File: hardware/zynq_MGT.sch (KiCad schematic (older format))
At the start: 6 parts, among them U201 xc7z030sbg485

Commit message: Layouted most of the Power Circuit and Triggerbus Levelshifters.
Added Footprint for Tantal Caps. Modified Footprint for MDR20 Connector, SD-Card.

Fixed Symbol and Circuit for Power Supervisor/Delay IC.

Also fixed some smaller things in the schematics.
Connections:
- wire segments 29 -> 30
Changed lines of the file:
@@
 $EndComp
 Wire Wire Line
-	5200 2150 5350 2150
+	5200 2150 5300 2150
 Wire Wire Line
 	5350 2650 4850 2650
@@
 	5300 1950 5300 2150
 Connection ~ 5300 2150
+Wire Wire Line
+	5300 2150 5350 2150
 $EndSCHEMATC

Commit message: Layouted USB-UART.
Also moved USB-OTG to the right Side of the Board. To get there
some free Space, i moved the DDR3/Memory and the FPGA a few
Millimeters down.
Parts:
- R1001: footprint (none) -> Resistor_SMD:R_0402_1005Metric
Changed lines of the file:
@@
 F 0 "R1001" H 5130 2170 50  0000 L CNN
 F 1 "100Ω, 1%" V 5000 1950 50  0000 L CNN
-F 2 "" H 5100 2150 50  0001 C CNN
+F 2 "Resistor_SMD:R_0402_1005Metric" H 5100 2150 50  0001 C CNN
 F 3 "" H 5100 2150 50  0001 C CNN
 	1    5100 2150

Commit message: Improved Powerdistribution Network of the FPGA.
Also started to layout USB.
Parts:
- C1001, C1002, C1003, C1004: footprint Capacitors_SMD:C_0402 -> Capacitor_SMD:C_0402_1005Metric
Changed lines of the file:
@@
 F 0 "C1004" H 4260 2620 50  0000 L CNN
 F 1 "C_Small" H 4260 2470 50  0000 L CNN
-F 2 "Capacitors_SMD:C_0402" H 4250 2550 50  0001 C CNN
+F 2 "Capacitor_SMD:C_0402_1005Metric" H 4250 2550 50  0001 C CNN
 F 3 "" H 4250 2550 50  0000 C CNN
 	1    4250 2550
@@
 F 0 "C1003" H 4010 2520 50  0000 L CNN
 F 1 "C_Small" H 4010 2370 50  0000 L CNN
-F 2 "Capacitors_SMD:C_0402" H 4000 2450 50  0001 C CNN
+F 2 "Capacitor_SMD:C_0402_1005Metric" H 4000 2450 50  0001 C CNN
 F 3 "" H 4000 2450 50  0000 C CNN
 	1    4000 2450
@@
 F 0 "C1001" H 3510 2320 50  0000 L CNN
 F 1 "C_Small" H 3510 2170 50  0000 L CNN
-F 2 "Capacitors_SMD:C_0402" H 3500 2250 50  0001 C CNN
+F 2 "Capacitor_SMD:C_0402_1005Metric" H 3500 2250 50  0001 C CNN
 F 3 "" H 3500 2250 50  0000 C CNN
 	1    3500 2250
@@
 F 0 "C1002" H 3760 2420 50  0000 L CNN
 F 1 "C_Small" H 3760 2270 50  0000 L CNN
-F 2 "Capacitors_SMD:C_0402" H 3750 2350 50  0001 C CNN
+F 2 "Capacitor_SMD:C_0402_1005Metric" H 3750 2350 50  0001 C CNN
 F 3 "" H 3750 2350 50  0000 C CNN
 	1    3750 2350

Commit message: Fixed Schematic Symbols
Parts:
- C1001, C1002, C1003, C1004: symbol device:C_Small -> Device:C_Small
- R1001: symbol device:R_Small -> Device:R_Small
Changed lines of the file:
@@
 $Descr A4 11693 8268
 encoding utf-8
-Sheet 10 22
+Sheet 10 21
 Title ""
 Date ""
@@
 MGTREFCLK_1_P
 $Comp
-L device:C_Small C1004
+L Device:C_Small C1004
 U 1 1 598A74A2
 P 4250 2550
@@
 $EndComp
 $Comp
-L device:C_Small C1003
+L Device:C_Small C1003
 U 1 1 598A7543
 P 4000 2450
@@
 $EndComp
 $Comp
-L device:C_Small C1001
+L Device:C_Small C1001
 U 1 1 598A7566
 P 3500 2250
@@
 $EndComp
 $Comp
-L device:C_Small C1002
+L Device:C_Small C1002
 U 1 1 598A75B1
 P 3750 2350
@@
 MGTX_TX_0_P
 $Comp
-L device:R_Small R1001
+L Device:R_Small R1001
 U 1 1 5ADF6841
 P 5100 2150

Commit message: Xaui lanes
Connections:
- net MGTX_RX_0_N: now also U201.AB9 (MGTXRXN2_112_N); no longer U201.AB7 (MGTXRXN0_112_N)
- net MGTX_RX_0_P: now also U201.AA9 (MGTXRXP2_112_P); no longer U201.AA7 (MGTXRXP0_112_P)
- net MGTX_RX_2_N: now also U201.AB7 (MGTXRXN0_112_N); no longer U201.AB9 (MGTXRXN2_112_N)
- net MGTX_RX_2_P: now also U201.AA7 (MGTXRXP0_112_P); no longer U201.AA9 (MGTXRXP2_112_P)
- net MGTX_TX_0_N: now also U201.AA5 (MGTXTXP2_112_P); no longer U201.AB3 (MGTXTXN0_112_N)
- net MGTX_TX_0_P: now also U201.AB5 (MGTXTXN2_112_N); no longer U201.AA3 (MGTXTXP0_112_P)
- net MGTX_TX_1_N: now also U201.W4 (MGTXTXP1_112_P); no longer U201.Y4 (MGTXTXN1_112_N)
- net MGTX_TX_1_P: now also U201.Y4 (MGTXTXN1_112_N); no longer U201.W4 (MGTXTXP1_112_P)
- net MGTX_TX_2_N: now also U201.AA3 (MGTXTXP0_112_P); no longer U201.AB5 (MGTXTXN2_112_N)
- net MGTX_TX_2_P: now also U201.AB3 (MGTXTXN0_112_N); no longer U201.AA5 (MGTXTXP2_112_P)
- net MGTX_TX_3_N: now also U201.W2 (MGTXTXP3_112_P); no longer U201.Y2 (MGTXTXN3_112_N)
- net MGTX_TX_3_P: now also U201.Y2 (MGTXTXN3_112_N); no longer U201.W2 (MGTXTXP3_112_P)
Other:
- note added: "Pair 2 and 0 have been swapped, to ease routing"
- note added: "TX Polarity has been swapped to ease routing"
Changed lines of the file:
@@
 	1    0    0    -1
 $EndComp
-Text HLabel 3300 2750 0    60   Input ~ 0
+Text HLabel 3300 2950 0    60   Input ~ 0
 MGTX_RX_0_N
 Text HLabel 3300 2850 0    60   Input ~ 0
 MGTX_RX_1_N
-Text HLabel 3300 2950 0    60   Input ~ 0
+Text HLabel 3300 2750 0    60   Input ~ 0
 MGTX_RX_2_N
 Text HLabel 3300 3050 0    60   Input ~ 0
 MGTX_RX_3_N
-Text HLabel 3300 3150 0    60   Input ~ 0
+Text HLabel 3300 3350 0    60   Input ~ 0
 MGTX_RX_0_P
 Text HLabel 3300 3250 0    60   Input ~ 0
 MGTX_RX_1_P
-Text HLabel 3300 3350 0    60   Input ~ 0
+Text HLabel 3300 3150 0    60   Input ~ 0
 MGTX_RX_2_P
 Text HLabel 3300 3450 0    60   Input ~ 0
 MGTX_RX_3_P
+Text HLabel 3300 4150 0    60   Output ~ 0
+MGTX_TX_0_N
+Text HLabel 3300 4050 0    60   Output ~ 0
+MGTX_TX_1_N
+Text HLabel 3300 3950 0    60   Output ~ 0
+MGTX_TX_2_N
+Text HLabel 3300 4250 0    60   Output ~ 0
+MGTX_TX_3_N
+Text HLabel 3300 3750 0    60   Output ~ 0
+MGTX_TX_0_P
+Text HLabel 3300 3650 0    60   Output ~ 0
+MGTX_TX_1_P
 Text HLabel 3300 3550 0    60   Output ~ 0
-MGTX_TX_0_N
-Text HLabel 3300 3650 0    60   Output ~ 0
-MGTX_TX_1_N
-Text HLabel 3300 3750 0    60   Output ~ 0
-MGTX_TX_2_N
+MGTX_TX_2_P
 Text HLabel 3300 3850 0    60   Output ~ 0
-MGTX_TX_3_N
-Text HLabel 3300 3950 0    60   Output ~ 0
-MGTX_TX_0_P
-Text HLabel 3300 4050 0    60   Output ~ 0
-MGTX_TX_1_P
-Text HLabel 3300 4150 0    60   Output ~ 0
-MGTX_TX_2_P
-Text HLabel 3300 4250 0    60   Output ~ 0
 MGTX_TX_3_P
 Text HLabel 3300 2250 0    60   Input ~ 0
@@
 	3300 2550 4150 2550
 Wire Wire Line
+	3300 2950 5350 2950
+Wire Wire Line
+	5350 2850 3300 2850
+Wire Wire Line
 	3300 2750 5350 2750
 Wire Wire Line
-	5350 2850 3300 2850
-Wire Wire Line
-	3300 2950 5350 2950
-Wire Wire Line
 	5350 3050 3300 3050
 Wire Wire Line
+	3300 3350 5350 3350
+Wire Wire Line
+	5350 3250 3300 3250
+Wire Wire Line
 	3300 3150 5350 3150
 Wire Wire Line
-	5350 3250 3300 3250
-Wire Wire Line
-	3300 3350 5350 3350
-Wire Wire Line
 	5350 3450 3300 3450
 Wire Wire Line
+	3300 4150 5350 4150
+Wire Wire Line
+	5350 4050 3300 4050
+Wire Wire Line
+	3300 3950 5350 3950
+Wire Wire Line
+	5350 4250 3300 4250
+Wire Wire Line
+	3300 3750 5350 3750
+Wire Wire Line
+	5350 3650 3300 3650
+Wire Wire Line
 	3300 3550 5350 3550
 Wire Wire Line
-	5350 3650 3300 3650
-Wire Wire Line
-	3300 3750 5350 3750
-Wire Wire Line
 	5350 3850 3300 3850
-Wire Wire Line
-	3300 3950 5350 3950
-Wire Wire Line
-	5350 4050 3300 4050
-Wire Wire Line
-	3300 4150 5350 4150
-Wire Wire Line
-	5350 4250 3300 4250
 Text Label 5250 2850 2    60   ~ 0
 MGTX_RX_1_N
-Text Label 5250 2950 2    60   ~ 0
+Text Label 5250 2750 2    60   ~ 0
 MGTX_RX_2_N
 Text Label 5250 3050 2    60   ~ 0
@@
 Text Label 5250 3250 2    60   ~ 0
 MGTX_RX_1_P
-Text Label 5250 3350 2    60   ~ 0
+Text Label 5250 3150 2    60   ~ 0
 MGTX_RX_2_P
 Text Label 5250 3450 2    60   ~ 0
 MGTX_RX_3_P
+Text Label 5250 4050 2    60   ~ 0
+MGTX_TX_1_N
+Text Label 5250 3950 2    60   ~ 0
+MGTX_TX_2_N
+Text Label 5250 4250 2    60   ~ 0
+MGTX_TX_3_N
 Text Label 5250 3650 2    60   ~ 0
-MGTX_TX_1_N
+MGTX_TX_1_P
+Text Label 5250 3550 2    60   ~ 0
+MGTX_TX_2_P
+Text Label 5250 3850 2    60   ~ 0
+MGTX_TX_3_P
+Text Label 5250 3350 2    60   ~ 0
+MGTX_RX_0_P
+Text Label 5250 2950 2    60   ~ 0
+MGTX_RX_0_N
+Text Label 5250 4150 2    60   ~ 0
+MGTX_TX_0_N
 Text Label 5250 3750 2    60   ~ 0
-MGTX_TX_2_N
-Text Label 5250 3850 2    60   ~ 0
-MGTX_TX_3_N
-Text Label 5250 4050 2    60   ~ 0
-MGTX_TX_1_P
-Text Label 5250 4150 2    60   ~ 0
-MGTX_TX_2_P
-Text Label 5250 4250 2    60   ~ 0
-MGTX_TX_3_P
-Text Label 5250 3150 2    60   ~ 0
-MGTX_RX_0_P
-Text Label 5250 2750 2    60   ~ 0
-MGTX_RX_0_N
-Text Label 5250 3550 2    60   ~ 0
-MGTX_TX_0_N
-Text Label 5250 3950 2    60   ~ 0
 MGTX_TX_0_P
 $Comp
@@
 Wire Wire Line
 	5300 2150 5350 2150
+Wire Notes Line
+	2550 3500 5300 3500
+Wire Notes Line
+	5300 3500 5300 4350
+Wire Notes Line
+	5300 4350 2550 4350
+Wire Notes Line
+	2550 4350 2550 3500
+Text Notes 3200 4500 0    50   ~ 0
+TX Polarity has been swapped to ease routing
+Text Notes 500  3100 0    50   ~ 0
+Pair 2 and 0 have been swapped, to ease routing
 $EndSCHEMATC

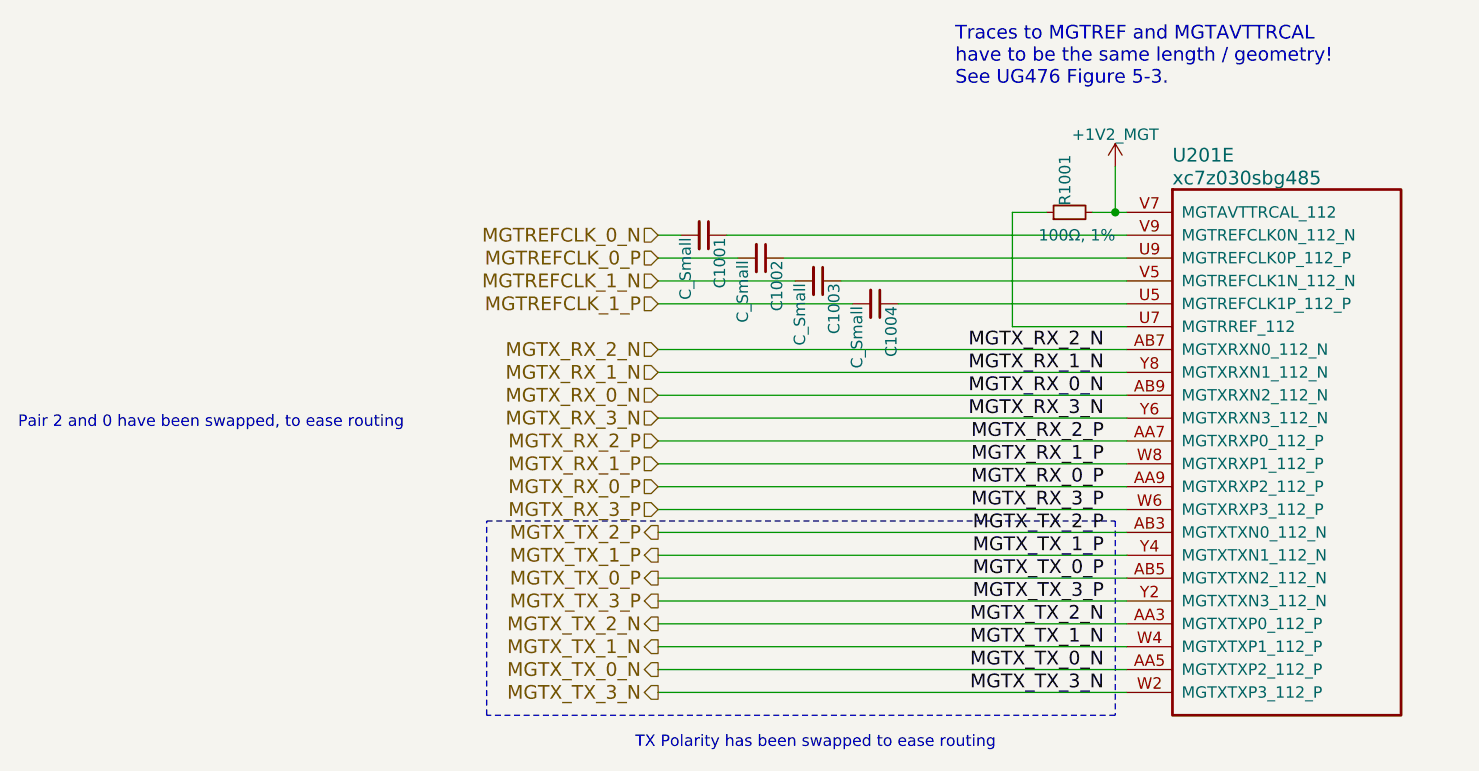
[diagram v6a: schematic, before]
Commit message: SFP+ Power Filter, Levelshifter and MGT/TLK Clock Distribution.
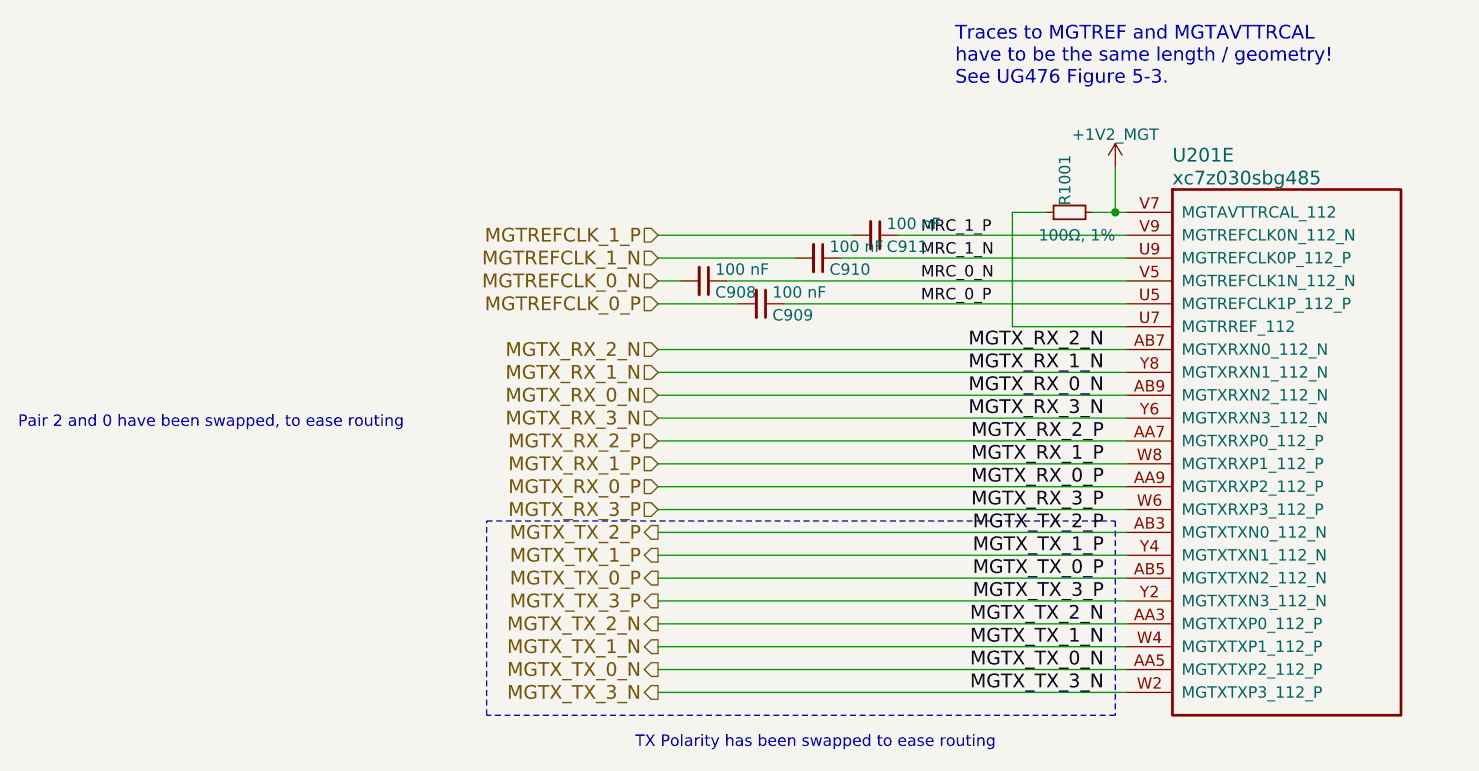
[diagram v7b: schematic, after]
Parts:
- removed C1001, C1002, C1003, C1004: C_Small, Capacitor_SMD:C_0402_1005Metric, symbol Device:C_Small
- added C908, C909, C910, C911: 100 nF, Capacitor_SMD:C_0201_0603Metric, symbol Device:C_Small
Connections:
- net MGTREFCLK_0_N: now also C908.2
- net MGTREFCLK_0_P: now also C909.2
- net MGTREFCLK_1_N: now also C910.2
- net MGTREFCLK_1_P: now also C911.2
- net MRC_0_P: now reaches U201.U5 (MGTREFCLK1P_112_P)
- net MRC_0_P: now also C909.1
- net MRC_1_N: now reaches U201.U9 (MGTREFCLK0P_112_P)
- net MRC_1_N: now also C910.1
- net MRC_0_N: now reaches U201.V5 (MGTREFCLK1N_112_N)
- net MRC_0_N: now also C908.1
- net MRC_1_P: now reaches U201.V9 (MGTREFCLK0N_112_N)
- net MRC_1_P: now also C911.1
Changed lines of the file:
@@
 Text HLabel 3300 3850 0    60   Output ~ 0
 MGTX_TX_3_P
+Text HLabel 3300 2450 0    60   Input ~ 0
+MGTREFCLK_0_N
+Text HLabel 3300 2550 0    60   Input ~ 0
+MGTREFCLK_0_P
+Text HLabel 3300 2350 0    60   Input ~ 0
+MGTREFCLK_1_N
 Text HLabel 3300 2250 0    60   Input ~ 0
-MGTREFCLK_0_N
-Text HLabel 3300 2350 0    60   Input ~ 0
-MGTREFCLK_0_P
-Text HLabel 3300 2450 0    60   Input ~ 0
-MGTREFCLK_1_N
-Text HLabel 3300 2550 0    60   Input ~ 0
 MGTREFCLK_1_P
-$Comp
-L Device:C_Small C1004
-U 1 1 598A74A2
-P 4250 2550
-F 0 "C1004" H 4260 2620 50  0000 L CNN
-F 1 "C_Small" H 4260 2470 50  0000 L CNN
-F 2 "Capacitor_SMD:C_0402_1005Metric" H 4250 2550 50  0001 C CNN
-F 3 "" H 4250 2550 50  0000 C CNN
-	1    4250 2550
-	0    1    1    0
-$EndComp
-$Comp
-L Device:C_Small C1003
-U 1 1 598A7543
-P 4000 2450
-F 0 "C1003" H 4010 2520 50  0000 L CNN
-F 1 "C_Small" H 4010 2370 50  0000 L CNN
-F 2 "Capacitor_SMD:C_0402_1005Metric" H 4000 2450 50  0001 C CNN
-F 3 "" H 4000 2450 50  0000 C CNN
-	1    4000 2450
-	0    1    1    0
-$EndComp
-$Comp
-L Device:C_Small C1001
-U 1 1 598A7566
-P 3500 2250
-F 0 "C1001" H 3510 2320 50  0000 L CNN
-F 1 "C_Small" H 3510 2170 50  0000 L CNN
-F 2 "Capacitor_SMD:C_0402_1005Metric" H 3500 2250 50  0001 C CNN
-F 3 "" H 3500 2250 50  0000 C CNN
-	1    3500 2250
-	0    1    1    0
-$EndComp
-$Comp
-L Device:C_Small C1002
-U 1 1 598A75B1
-P 3750 2350
-F 0 "C1002" H 3760 2420 50  0000 L CNN
-F 1 "C_Small" H 3760 2270 50  0000 L CNN
-F 2 "Capacitor_SMD:C_0402_1005Metric" H 3750 2350 50  0001 C CNN
-F 3 "" H 3750 2350 50  0000 C CNN
-	1    3750 2350
-	0    1    1    0
-$EndComp
-Wire Wire Line
-	3600 2250 5350 2250
-Wire Wire Line
-	3850 2350 5350 2350
-Wire Wire Line
-	4100 2450 5350 2450
-Wire Wire Line
-	4350 2550 5350 2550
-Wire Wire Line
-	3300 2250 3400 2250
-Wire Wire Line
-	3300 2350 3650 2350
-Wire Wire Line
-	3300 2450 3900 2450
-Wire Wire Line
-	3300 2550 4150 2550
+Wire Wire Line
+	3600 2450 5350 2450
+Wire Wire Line
+	3850 2550 5350 2550
+Wire Wire Line
+	4100 2350 5350 2350
+Wire Wire Line
+	4350 2250 5350 2250
+Wire Wire Line
+	3300 2450 3400 2450
+Wire Wire Line
+	3300 2550 3650 2550
+Wire Wire Line
+	3300 2350 3900 2350
+Wire Wire Line
+	3300 2250 4150 2250
 Wire Wire Line
 	3300 2950 5350 2950
@@
 Text Notes 500  3100 0    50   ~ 0
 Pair 2 and 0 have been swapped, to ease routing
+$Comp
+L Device:C_Small C908
+U 1 1 5BB22AAD
+P 3500 2450
+F 0 "C908" V 3550 2500 50  0000 L CNN
+F 1 "100 nF" V 3450 2500 50  0000 L CNN
+F 2 "Capacitor_SMD:C_0201_0603Metric" H 3500 2450 50  0001 C CNN
+F 3 "http://search.murata.co.jp/Ceramy/image/img/A01X/G101/ENG/GRM033R60J104KE19-01.pdf" H 3500 2450 50  0001 C CNN
+F 4 "Murata Electronics North America" H 3500 2450 60  0001 C CNN "MFG Name"
+F 5 "GRM033R60J104KE19D" H 3500 2450 60  0001 C CNN "MFG Part Num"
+F 6 "490-3167-1-ND" H 3500 2450 60  0001 C CNN "Digikey"
+F 7 "1" V 3500 2450 60  0001 C CNN "Populated"
+F 8 "SPEC" H 3500 2450 60  0001 C CNN "Source"
+	1    3500 2450
+	0    1    1    0
+$EndComp
+$Comp
+L Device:C_Small C909
+U 1 1 5BB23111
+P 3750 2550
+F 0 "C909" V 3800 2600 50  0000 L CNN
+F 1 "100 nF" V 3700 2600 50  0000 L CNN
+F 2 "Capacitor_SMD:C_0201_0603Metric" H 3750 2550 50  0001 C CNN
+F 3 "http://search.murata.co.jp/Ceramy/image/img/A01X/G101/ENG/GRM033R60J104KE19-01.pdf" H 3750 2550 50  0001 C CNN
+F 4 "Murata Electronics North America" H 3750 2550 60  0001 C CNN "MFG Name"
+F 5 "GRM033R60J104KE19D" H 3750 2550 60  0001 C CNN "MFG Part Num"
+F 6 "490-3167-1-ND" H 3750 2550 60  0001 C CNN "Digikey"
+F 7 "1" V 3750 2550 60  0001 C CNN "Populated"
+F 8 "SPEC" H 3750 2550 60  0001 C CNN "Source"
+	1    3750 2550
+	0    1    1    0
+$EndComp
+$Comp
+L Device:C_Small C910
+U 1 1 5BB23143
+P 4000 2350
+F 0 "C910" V 4050 2400 50  0000 L CNN
+F 1 "100 nF" V 3950 2400 50  0000 L CNN
+F 2 "Capacitor_SMD:C_0201_0603Metric" H 4000 2350 50  0001 C CNN
+F 3 "http://search.murata.co.jp/Ceramy/image/img/A01X/G101/ENG/GRM033R60J104KE19-01.pdf" H 4000 2350 50  0001 C CNN
+F 4 "Murata Electronics North America" H 4000 2350 60  0001 C CNN "MFG Name"
+F 5 "GRM033R60J104KE19D" H 4000 2350 60  0001 C CNN "MFG Part Num"
+F 6 "490-3167-1-ND" H 4000 2350 60  0001 C CNN "Digikey"
+F 7 "1" V 4000 2350 60  0001 C CNN "Populated"
+F 8 "SPEC" H 4000 2350 60  0001 C CNN "Source"
+	1    4000 2350
+	0    1    1    0
+$EndComp
+$Comp
+L Device:C_Small C911
+U 1 1 5BB231AA
+P 4250 2250
+F 0 "C911" V 4300 2300 50  0000 L CNN
+F 1 "100 nF" V 4200 2300 50  0000 L CNN
+F 2 "Capacitor_SMD:C_0201_0603Metric" H 4250 2250 50  0001 C CNN
+F 3 "http://search.murata.co.jp/Ceramy/image/img/A01X/G101/ENG/GRM033R60J104KE19-01.pdf" H 4250 2250 50  0001 C CNN
+F 4 "Murata Electronics North America" H 4250 2250 60  0001 C CNN "MFG Name"
+F 5 "GRM033R60J104KE19D" H 4250 2250 60  0001 C CNN "MFG Part Num"
+F 6 "490-3167-1-ND" H 4250 2250 60  0001 C CNN "Digikey"
+F 7 "1" V 4250 2250 60  0001 C CNN "Populated"
+F 8 "SPEC" H 4250 2250 60  0001 C CNN "Source"
+	1    4250 2250
+	0    1    1    0
+$EndComp
+Text Label 4450 2250 0    50   ~ 0
+MRC_1_P
+Text Label 4450 2350 0    50   ~ 0
+MRC_1_N
+Text Label 4450 2550 0    50   ~ 0
+MRC_0_P
+Text Label 4450 2450 0    50   ~ 0
+MRC_0_N
 $EndSCHEMATC
